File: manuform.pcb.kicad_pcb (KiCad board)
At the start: 2 copper layers, 100 x 90 mm, 48 parts, among them J1 Conn_01x04, J2 Conn_01x04, J3 Conn_01x04, SW1 SW_DIP_x01, SW2 SW_DIP_x01, SW3 SW_DIP_x01, SW4 SW_DIP_x01

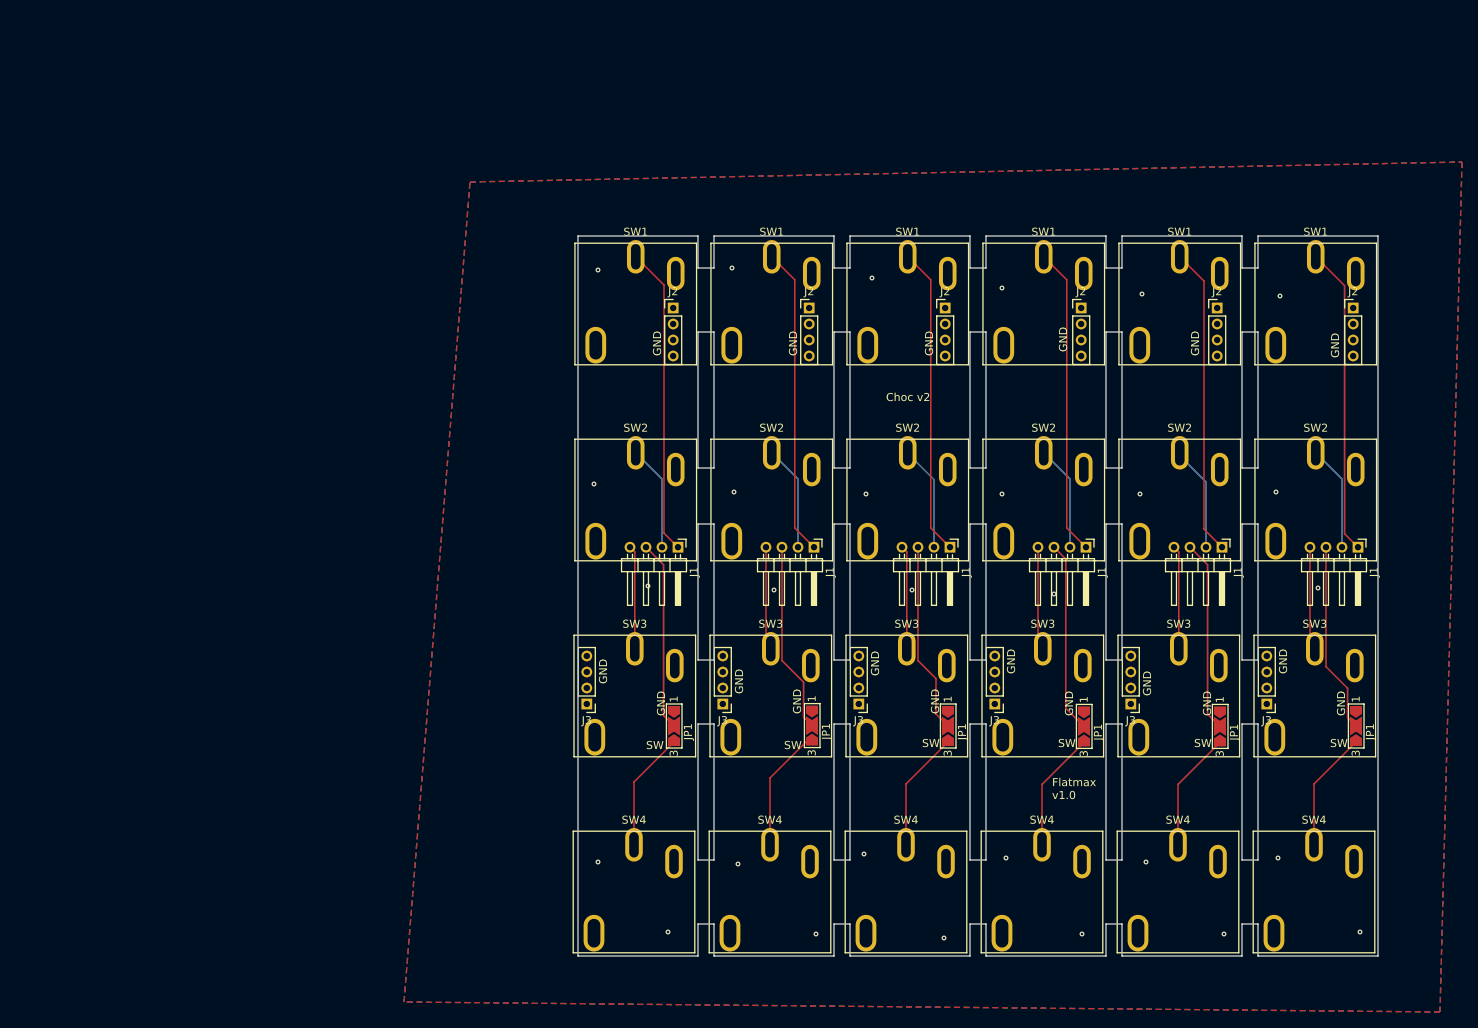
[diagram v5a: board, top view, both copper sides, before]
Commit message: added MX diodeless switches.
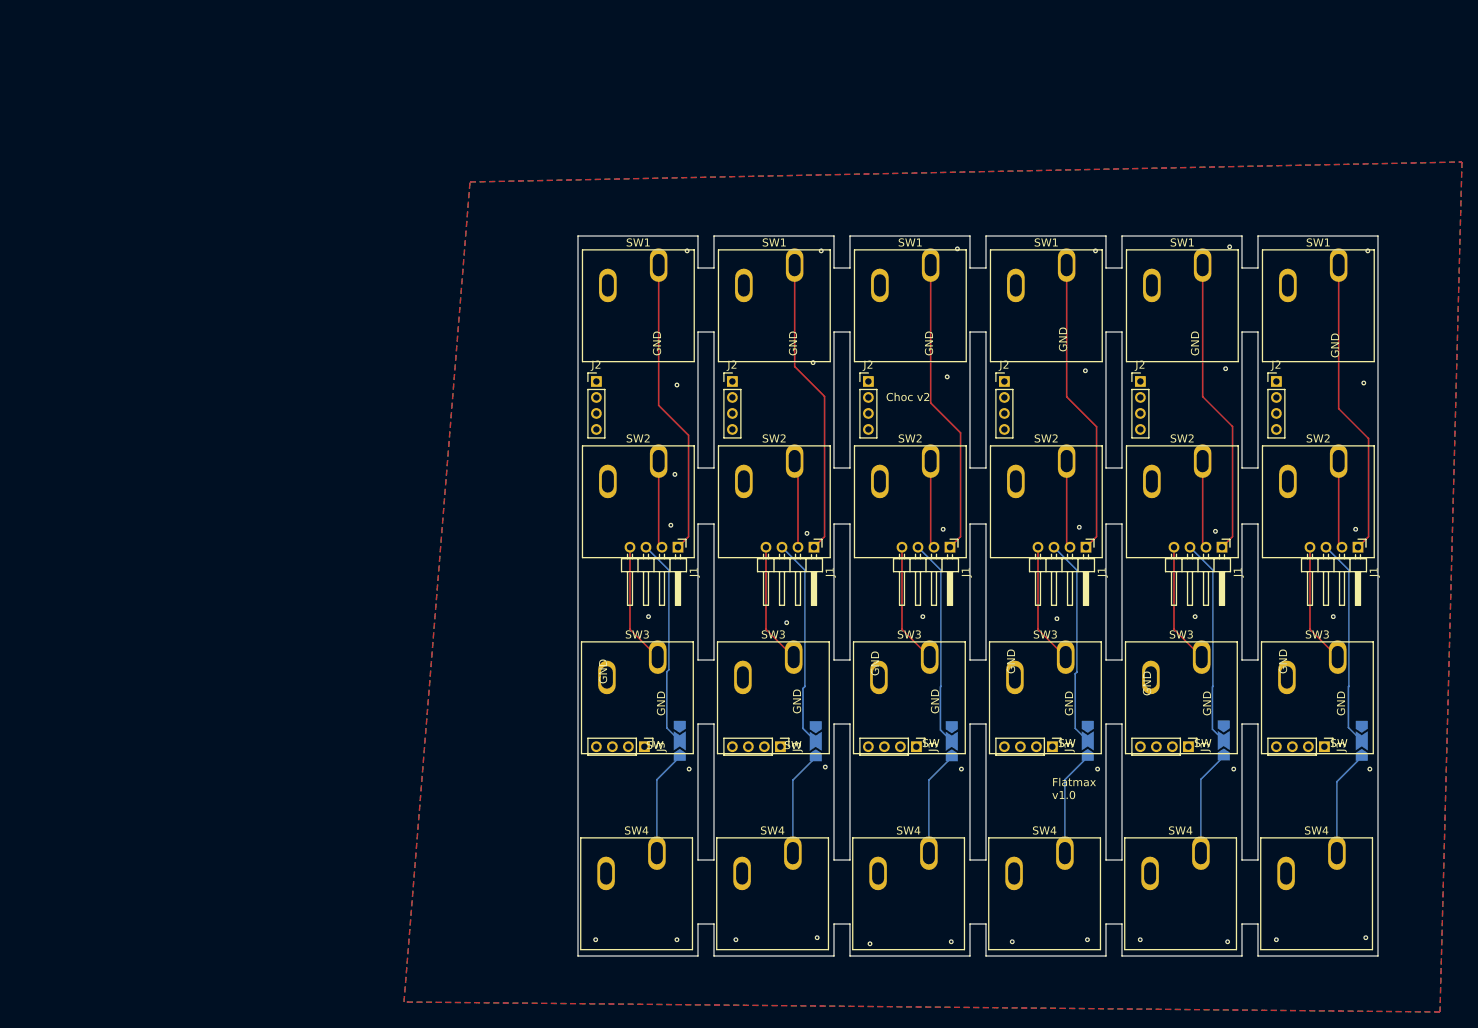
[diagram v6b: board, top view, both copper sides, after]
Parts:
- JP1 (x6): moved to B.Cu
- SW1 (x6), SW2 (x6), SW3 (x6), SW4 (x6): footprint switchCustom:SW_Kailh_Choc_V2_elongated -> switchCustom:SW_Cherry_MX_1.00u_PCB
- moved JP1 86.0 mm to (252.0, 100.1)
- moved JP1 84.6 mm to (166.7, 100.1)
- moved JP1 51.5 mm to (234.7, 100.1)
- moved JP1 50.6 mm to (183.7, 100.2)
- moved JP1 17.6 mm to (217.7, 100.1)
- moved JP1 16.6 mm to (200.7, 100.2)
- moved J2 13.3 mm to (207.3, 55.2)
- moved J2 13.3 mm to (241.3, 55.2)
- moved J2 13.3 mm to (173.3, 55.2)
- moved J2 13.3 mm to (156.3, 55.2)
- moved J2 13.3 mm to (224.3, 55.2)
- moved J2 13.3 mm to (190.3, 55.2)
- moved J3 8.96 mm to (247.3, 100.8), turned to -90 degrees
- moved J3 8.96 mm to (162.3, 100.8), turned to -90 degrees
- moved J3 8.96 mm to (230.3, 100.8), turned to -90 degrees
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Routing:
- net Net-(J1-Pin_2): track 79.0 -> 65.6 mm
- net Net-(J1-Pin_4): track 77.7 -> 91.0 mm
- net Net-(J1-Pin_3): track 143.4 -> 156.6 mm
- net Net-(JP1-B): track 90.4 -> 79.3 mm
- net Net-(J1-Pin_1): track 230.9 -> 224.1 mm
- net GND: vias 29 -> 43
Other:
- board text added: "1 2 4 3"
